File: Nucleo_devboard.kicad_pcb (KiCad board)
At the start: 4 copper layers, 70 x 82.5 mm, 62 parts, among them J2 Conn_ST_STDC14, J3 USB_5V, J4 E5V, J5 Curr_measure, J6 USB4105-GF-A, SW2 BOOT0 pull, U1 STM32G474RETx, U2 USBLC6-2SC6, U3 CP2102C-Axx-xQFN24, U4 NUCLEO-G474RE, U5 TLV75533PDBV, Y1 Crystal 24MHz, Y2 Crystal 32.768KHz

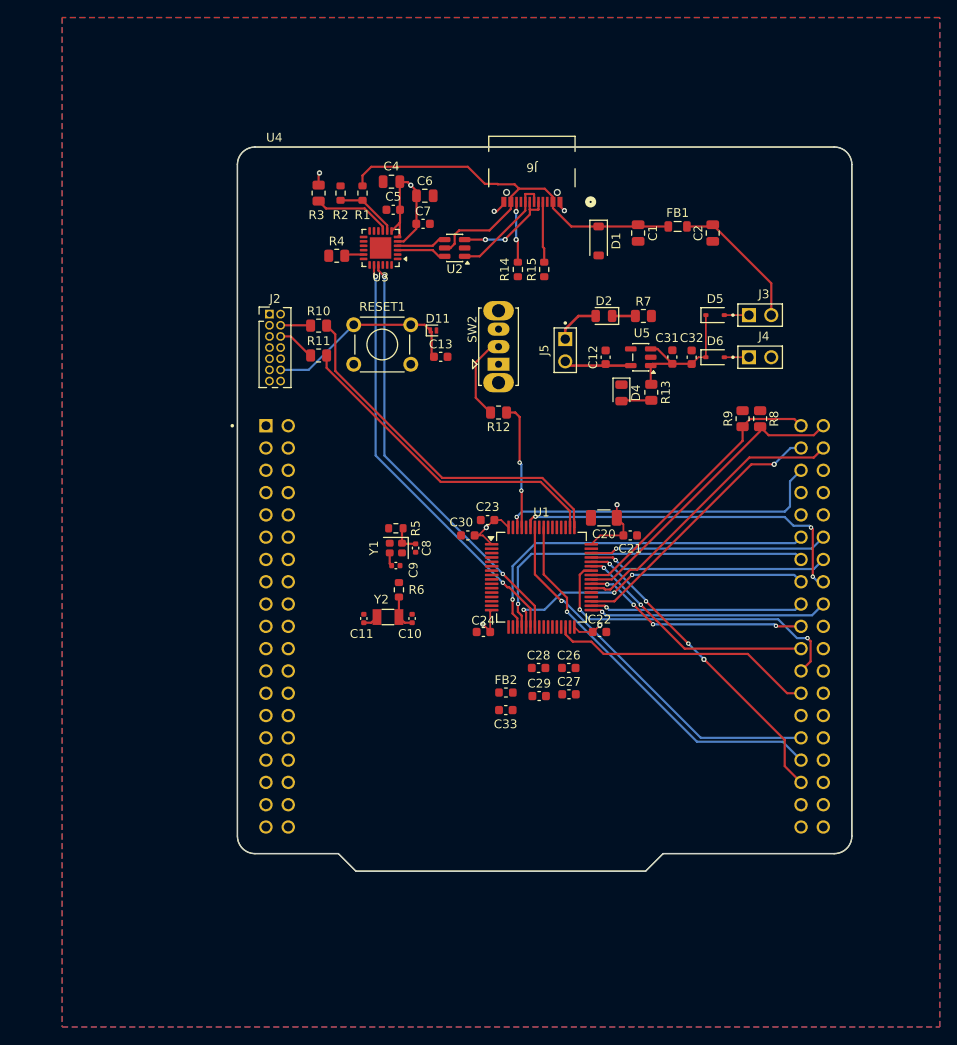
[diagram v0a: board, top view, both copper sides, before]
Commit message: Added Current reading for INA228 Started rev 02 on brake sense
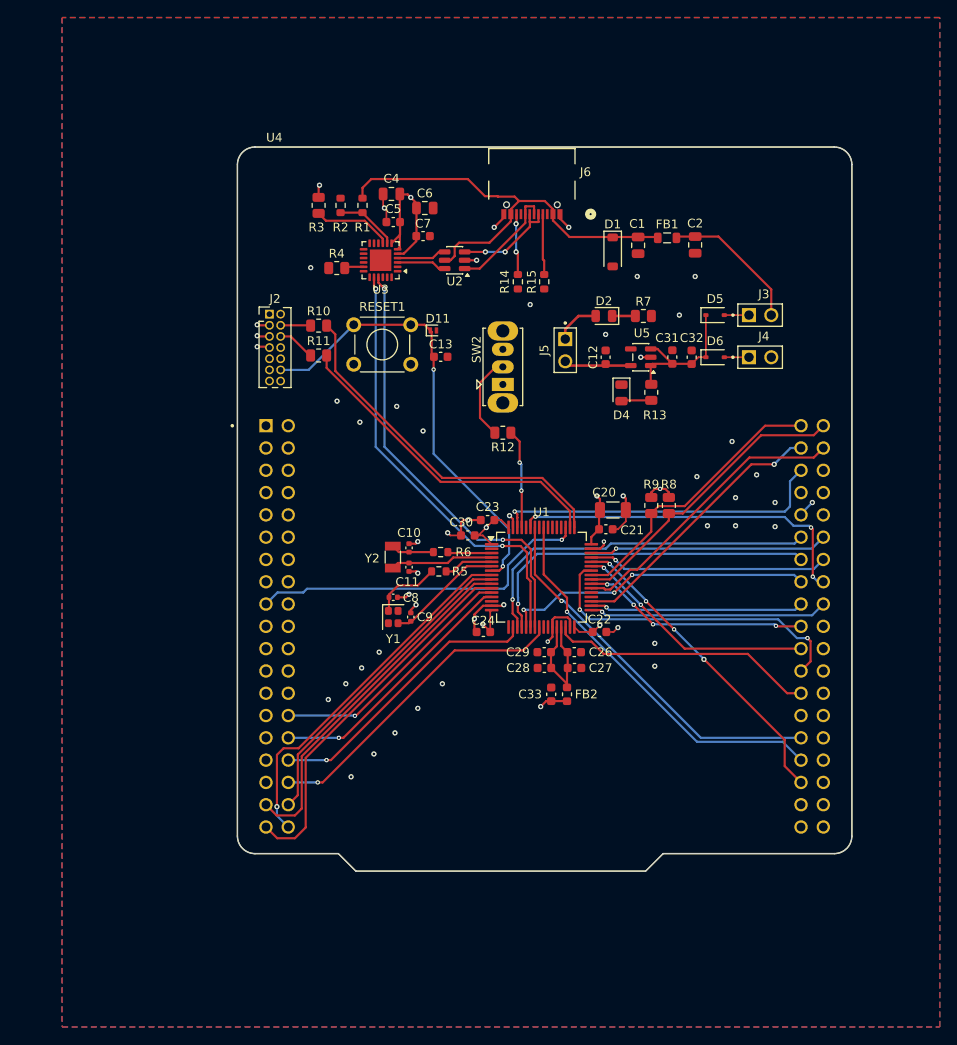
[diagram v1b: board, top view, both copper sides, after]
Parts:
- moved R8 14.4 mm to (155.4, 104.1)
- moved R9 14.4 mm to (153.4, 104.1)
- moved C10 8.05 mm to (125.8, 108.9)
- moved Y1 7.87 mm to (124.0, 116.8), turned to -90 degrees
- moved C11 7.79 mm to (125.8, 111.1), turned to 90 degrees
- moved FB2 6.97 mm to (143.8, 125.6), turned to 90 degrees
- moved R5 6.94 mm to (129.2, 111.6), turned to 0 degrees
- moved Y2 6.85 mm to (124.0, 110.0), turned to 90 degrees
- moved R6 6.40 mm to (129.4, 109.4), turned to 0 degrees
- moved C8 6.16 mm to (124.0, 114.5), turned to 180 degrees
- moved C9 6.10 mm to (126.0, 116.8), turned to -90 degrees
- moved C33 5.48 mm to (142.0, 125.6), turned to 90 degrees
- moved C29 5.03 mm to (141.2, 120.8), turned to 180 degrees
- moved C27 3.06 mm to (144.7, 122.6)
- moved C21 2.86 mm to (148.2, 106.8)
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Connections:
- R8 pad 2: GND -> +3V3
- R9 pad 2: GND -> +3V3
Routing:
- net GND: track 2.91 -> 46.7 mm, vias 2 -> 42
- net /MCU/SNS_ARMREST: track 0.00 -> 42.7 mm
- net /MCU/EN_ARMREST: track 0.00 -> 41.7 mm, vias 0 -> 1
- net /MCU/BTN_CDC: track 0.00 -> 40.6 mm
- net /MCU/FD_CAN3_TX: track 0.00 -> 39.6 mm, vias 0 -> 1
- net /MCU/EN_CDC: track 0.00 -> 36.5 mm
- net /MCU/ADC_LIFT_A: track 0.00 -> 36.4 mm, vias 0 -> 1
- net /MCU/ADC_TILT_A: track 0.00 -> 32.5 mm, vias 0 -> 1
- net /MCU/ADC_STEER_A: track 0.00 -> 29.8 mm, vias 0 -> 1
- net /MCU/NRST: track 22.6 -> 51.9 mm, vias 0 -> 2
- net /MCU/ADC_THROTTLE_A: track 0.00 -> 29.0 mm, vias 0 -> 1
- net VDDA: track 0.00 -> 15.1 mm
- net /MCU/HSE_OUT: track 1.54 -> 13.4 mm
- net /MCU/LSE_OUT: track 1.77 -> 11.8 mm
- net +3V3: track 46.2 -> 52.5 mm, vias 6 -> 17
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
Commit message: added rev04_mcu1/2.h revised brake sense board Added logic for 2 MCUs on nucleo board
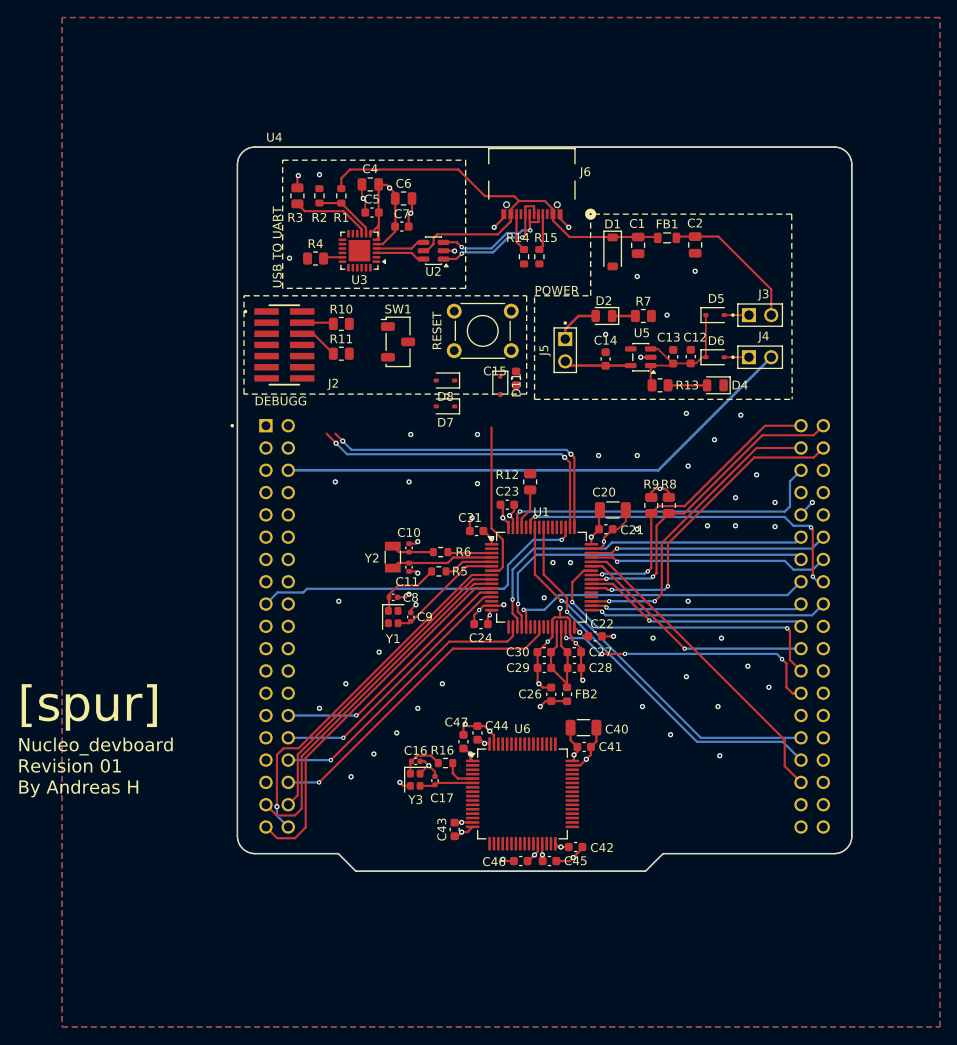
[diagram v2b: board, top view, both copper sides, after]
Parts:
- removed the C31 at (155.8, 87.2)
- removed C32: 1μF, Capacitor_SMD:C_0603_1608Metric
- removed SW2: BOOT0 pull, Button_Switch_THT:SW_Slide_SPDT_Straight_CK_OS102011MS2Q
- added C13: 100nF, Capacitor_SMD:C_0603_1608Metric, F.Cu at (155.9, 87.2)
- added C14: 1μF, Capacitor_SMD:C_0603_1608Metric, F.Cu at (148.2, 87.4)
- added C16: 6.8pF, Capacitor_SMD:C_0402_1005Metric, F.Cu at (126.6, 133.2)
- added C17: 6.8pF, Capacitor_SMD:C_0402_1005Metric, F.Cu at (128.8, 135.4)
- added C40: 10μF, Capacitor_SMD:C_1206_3216Metric, F.Cu at (145.7, 129.4)
- added C41: 100nF, Capacitor_SMD:C_0603_1608Metric, F.Cu at (145.8, 131.6)
- added C42: 100nF, Capacitor_SMD:C_0603_1608Metric, F.Cu at (144.8, 143.0)
- added C43: 100nF, Capacitor_SMD:C_0603_1608Metric, F.Cu at (131.0, 141.0)
- added C44: 100nF, Capacitor_SMD:C_0603_1608Metric, F.Cu at (133.6, 130.0)
- added C45: 100nF, Capacitor_SMD:C_0603_1608Metric, F.Cu at (141.8, 144.6)
- added C46: 100nF, Capacitor_SMD:C_0603_1608Metric, F.Cu at (138.5, 144.6)
- added C47: 100nF, Capacitor_SMD:C_0603_1608Metric, F.Cu at (132.0, 131.0)
- added D7: BAT60A, Diode_SMD:D_SOD-323, F.Cu at (129.9, 92.8)
- added D8: BAT60A, Diode_SMD:D_SOD-323, F.Cu at (129.9, 89.8)
- added R16: 0, Resistor_SMD:R_0603_1608Metric, F.Cu at (130.0, 133.4)
- added SW1: SW_Nidec_CAS-120A1, Button_Switch_SMD:Nidec_Copal_CAS-120A, F.Cu at (124.5, 85.5)
- added U6: STM32G474RETx, Package_QFP:LQFP-64_10x10mm_P0.5mm, F.Cu at (138.7, 136.9)
- added Y3: Crystal 24MHz, Crystal:Crystal_SMD_2016-4Pin_2.0x1.6mm, F.Cu at (126.5, 135.3)
- D11: value PESD3V3U1UL -> CDSOD323-T03; footprint Diode_SMD:D_SOD-882 -> Diode_SMD:D_SOD-323
- D5, D6: value SS34 -> BAT60A
- J2: value Conn_ST_STDC14 -> st_debug_SMD; footprint Connector_PinHeader_1.27mm:PinHeader_2x07_P1.27mm_Vertical -> tinynav:PinHeader_2x07_P1.27mm_Vertical_SMD
- moved RESET1 11.6 mm to (130.9, 82.0)
- moved D4 10.7 mm to (160.7, 90.4), turned to 180 degrees
- moved D11 9.86 mm to (136.2, 90.4), turned to -90 degrees
- moved C12 9.70 mm to (157.9, 87.1)
- moved C15 8.93 mm to (138.0, 89.6), turned to -90 degrees
- moved R12 6.41 mm to (139.6, 101.4), turned to 90 degrees
- moved J2 3.90 mm to (111.6, 85.8), turned to -90 degrees
- moved R14 2.93 mm to (138.9, 75.8)
- moved R15 2.90 mm to (140.7, 75.8)
- moved C23 2.85 mm to (137.0, 104.0), turned to 0 degrees
- moved C7 2.65 mm to (125.0, 72.3)
- moved C6 2.65 mm to (125.2, 69.1)
- moved R1 2.65 mm to (118.1, 68.8)
- moved R2 2.65 mm to (115.6, 68.8)
- moved R3 2.65 mm to (113.1, 68.8)
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- renumbered C13 to C15, C33 to C26, C26 to C27, C27 to C28, C28 to C29, C29 to C30, C30 to C31
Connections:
- net /MCU/E5V renamed /Morpho connector/E5V
- net /MCU/SWCLK renamed MCU2_SWDCLK
- net /MCU/USB/USB_5V renamed /Power/USB_5V
- net /MCU/USB/VBUS_DETECT renamed /USB/VBUS_DETECT
- C12 pad 1: /MCU/3.3V_OUT -> +5V
- J2 pad 11: unconnected-(J2-GNDDetect-Pad11) -> GND
- J5 pad 2: /MCU/3.3V_OUT -> /Power/3.3V_OUT
- R10 pad 2: /MCU/SWDIO -> Net-(SW1-B)
- R12 pad 2: Net-(SW2-B) -> GND
- RESET1 pad 1: /MCU/NRST -> Net-(D7-K)
- U1 pad 22: USART1_TX -> /MCU/USART_1TX
- U1 pad 23: USART1_RX -> /MCU/USART1_RX
- U1 pad 52: unconnected-(U1-PC10-Pad52) -> /MCU/USART3_TX
- U1 pad 53: unconnected-(U1-PC11-Pad53) -> /MCU/USART3_RX
- U3 pad 20: USART1_TX -> /MCU/USART3_RX
- U3 pad 21: USART1_RX -> /MCU/USART3_TX
- U5 pad 5: /MCU/3.3V_OUT -> /Power/3.3V_OUT
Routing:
- net USART1_TX: track 50.3 -> 0.00 mm, vias 2 -> 0
- net USART1_RX: track 50.2 -> 0.00 mm, vias 2 -> 0
- net GND: track 46.7 -> 82.7 mm, vias 42 -> 76
- net /MCU/NRST: track 51.9 -> 17.9 mm, vias 2 -> 0
- net Net-(SW2-B): track 9.74 -> 0.00 mm
- net +3V3: track 52.5 -> 60.3 mm, vias 17 -> 16
- net /Power/3.3V_OUT: track 0.00 -> 7.66 mm
- net /MCU/3.3V_OUT: track 7.66 -> 0.00 mm
- net /MCU/BOOT: track 11.3 -> 4.67 mm, vias 2 -> 0
- net /MCU 2/HSE_OUT: track 0.00 -> 6.13 mm
- net Net-(C16-Pad2): track 0.00 -> 5.12 mm
- net /MCU/SWDIO: track 41.4 -> 36.3 mm, vias 0 -> 2
- net VBUS: track 51.4 -> 56.1 mm
- net /MCU 2/HSE_IN: track 0.00 -> 3.68 mm
- net /MCU/EN_PARK_N: track 31.1 -> 34.6 mm, vias 1 -> 2
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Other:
- board text added: "DEBUGG"
- board text added: "Nucleo_devboard Revision 01 By Andreas H"
- board text added: "POWER"
- board text added: "RESET"
- board text added: "USB TO UART"
- board text added: "[spur]"

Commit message: Generated scaffold for mcu2 finished brake sense rev2 finished adding second chip to nucleo devboard
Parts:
- removed SW1: SW_Nidec_CAS-120A1, Button_Switch_SMD:Nidec_Copal_CAS-120A
- added C18: 100nF, Capacitor_SMD:C_0603_1608Metric, F.Cu at (133.0, 129.8)
- added C50: 100nF, Capacitor_SMD:C_0603_1608Metric, F.Cu at (152.0, 139.4)
- added C51: 100nF, Capacitor_SMD:C_0603_1608Metric, F.Cu at (155.4, 139.4)
- added D12: CDSOD323-T03, Diode_SMD:D_SOD-323, F.Cu at (127.8, 89.4)
- added J1: st_debug_SMD, tinynav:PinHeader_2x07_P1.27mm_Vertical_SMD, F.Cu at (111.2, 74.8)
- added J7: Conn_01x03_Socket, tinynav:DF3-3P-2DSA, F.Cu at (162.9, 136.5)
- added J8: CAN, tinynav:HARWIN_M20-9990246, F.Cu at (159.2, 135.2)
- added R17: 47, Resistor_SMD:R_0805_2012Metric, F.Cu at (118.1, 87.1)
- added R18: 47, Resistor_SMD:R_0805_2012Metric, F.Cu at (118.1, 89.4)
- added R29: 120, Resistor_SMD:R_0805_2012Metric, F.Cu at (159.2, 139.2)
- added U7: MCP2562-E-SN, Package_SO:SOIC-8_3.9x4.9mm_P1.27mm, F.Cu at (153.6, 135.8)
- RESET1: value SW_SPST -> RST_button
- moved C15 15.0 mm to (133.7, 104.0), turned to 180 degrees
- moved D11 11.6 mm to (127.8, 82.4), turned to 0 degrees
- moved D7 8.30 mm to (127.8, 84.8)
- moved R3 6.22 mm to (119.3, 68.6)
- moved C6 5.90 mm to (131.1, 69.0)
- moved C4 5.90 mm to (127.3, 67.4)
- moved C5 5.90 mm to (127.5, 70.6)
- moved C7 5.90 mm to (130.9, 72.2)
- moved R1 5.90 mm to (124.0, 68.7)
- moved R2 5.90 mm to (121.5, 68.7)
- moved R4 5.90 mm to (121.0, 75.9)
- moved U3 5.90 mm to (126.0, 75.0)
- moved FB1 4.84 mm to (154.2, 78.3), turned to -90 degrees
- moved C2 4.39 mm to (156.6, 78.4), turned to 90 degrees
- moved C1 3.91 mm to (151.6, 78.3)
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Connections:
- net /MCU/ADC_BRAKE renamed /MCU 1/ADC_BRAKE
- net /MCU/ADC_LIFT_A renamed /MCU 1/ADC_LIFT_A
- net /MCU/ADC_STEER_A renamed /MCU 1/ADC_STEER_A
- net /MCU/ADC_THROTTLE_A renamed /MCU 1/ADC_THROTTLE_A
- net /MCU/ADC_TILT_A renamed /MCU 1/ADC_TILT_A
- net /MCU/BTN_CDC renamed /MCU 1/BTN_CDC
- net /MCU/BTN_FNR_F renamed /MCU 1/BTN_FNR_F
- net /MCU/BTN_FNR_R renamed /MCU 1/BTN_FNR_R
- net /MCU/BTN_KICK renamed /MCU 1/BTN_KICK
- net /MCU/EN_ARMREST renamed /MCU 1/EN_ARMREST
- net /MCU/EN_CDC renamed /MCU 1/EN_CDC
- net /MCU/EN_FNR_F renamed /MCU 1/EN_FNR_F
- net /MCU/EN_FNR_R renamed /MCU 1/EN_FNR_R
- net /MCU/EN_KICK renamed /MCU 1/EN_KICK
- net /MCU/FDCAN2_TX renamed /MCU 1/FDCAN2_TX
- net /MCU/FD_CAN1_RX renamed /MCU 1/FD_CAN1_RX
- net /MCU/FD_CAN1_TX renamed /MCU 1/FD_CAN1_TX
- net /MCU/FD_CAN2_RX renamed /MCU 1/FD_CAN2_RX
- net /MCU/FD_CAN3_RX renamed /MCU 1/FD_CAN3_RX
- net /MCU/FD_CAN3_TX renamed /MCU 1/FD_CAN3_TX
- net /MCU/HSE_IN renamed /MCU 1/HSE_IN
- net /MCU/HSE_OUT renamed /MCU 1/HSE_OUT
- net /MCU/I2C_SCL renamed /MCU 1/I2C_SCL
- net /MCU/I2C_SDA renamed /MCU 1/I2C_SDA
- net /MCU/LDAC_LIFT_TILT renamed /MCU 1/LDAC_LIFT_TILT
- net /MCU/LDAC_STEER renamed /MCU 1/LDAC_STEER
- net /MCU/LDAC_THROTTLE renamed /MCU 1/LDAC_THROTTLE
- net /MCU/LSE_IN renamed /MCU 1/LSE_IN
- net /MCU/LSE_OUT renamed /MCU 1/LSE_OUT
- net /MCU/PWM_BRAKE renamed /MCU 1/PWM_BRAKE
- net /MCU/SEL_INJECT renamed /MCU 1/SEL_INJECT
- net /MCU/SNS_ARMREST renamed /MCU 1/SNS_ARMREST
- net /MCU/USART3_RX renamed /MCU 1/USART3_RX
- net /MCU/USART3_TX renamed /MCU 1/USART3_TX
- net MCU2_SWDCLK renamed /MCU 1/SWCLK1
- C15 pad 1: /MCU/NRST -> /MCU 1/NRST
- D11 pad 1: /MCU/NRST -> /MCU 1/NRST
- D7 pad 2: /MCU/NRST -> /MCU 1/NRST
- D8 pad 2: MCU2_rst -> /MCU 2/NRST
- J2 pad 12: /MCU/NRST -> /MCU 2/NRST
- R10 pad 1: Net-(J2-JTMS/SWDIO) -> Net-(J1-JTMS/SWDIO)
- R10 pad 2: Net-(SW1-B) -> /MCU 1/SWDIO1
- R11 pad 1: Net-(J2-JCLK/SWCLK) -> Net-(J1-JCLK/SWCLK)
- R12 pad 1: /MCU/BOOT -> /MCU 1/BOOT
- U1 pad 22: /MCU/USART_1TX -> /MCU 1/USART_1TX
- U1 pad 23: /MCU/USART1_RX -> /MCU 1/USART1_RX
- U1 pad 35: /MCU/EN_PARK_N -> unconnected-(U1-PB13-Pad35)
- U1 pad 49: /MCU/SWDIO -> /MCU 1/SWDIO1
- U1 pad 61: /MCU/BOOT -> /MCU 1/BOOT
- U1 pad 7: /MCU/NRST -> /MCU 1/NRST
- U4 pad CN10_3: /MCU/EN_PARK_N -> /MCU 1/BOOT
- U4 pad CN7_16: +3.3V -> +3V3
- U6 pad 45: unconnected-(U6-PA11-Pad45) -> /MCU 2/FC_CAN1_RX
- U6 pad 46: unconnected-(U6-PA12-Pad46) -> /MCU 2/FC_CAN1_TX
- U6 pad 49: unconnected-(U6-PA13-Pad49) -> /MCU 2/SWDIO2
- U6 pad 50: unconnected-(U6-PA14-Pad50) -> /MCU 2/SWCLK2
- U6 pad 52: unconnected-(U6-PC10-Pad52) -> /MCU 1/USART1_RX
- U6 pad 53: unconnected-(U6-PC11-Pad53) -> /MCU 1/USART_1TX
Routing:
- net +5V: track 16.8 -> 107.5 mm, vias 0 -> 2
- net /MCU 2/NRST: track 0.00 -> 74.1 mm, vias 0 -> 5
- net /MCU 2/SWDIO2: track 0.00 -> 65.3 mm, vias 0 -> 2
- net /MCU 2/SWCLK2: track 0.00 -> 62.4 mm, vias 0 -> 2
- net /MCU 1/NRST: track 0.00 -> 57.9 mm, vias 0 -> 4
- net /MCU 1/SWDIO1: track 0.00 -> 48.2 mm, vias 0 -> 2
- net /MCU 1/USART3_TX: track 0.00 -> 45.3 mm, vias 0 -> 2
- net /MCU 1/USART3_RX: track 0.00 -> 45.2 mm, vias 0 -> 2
- net GND: track 82.7 -> 122.1 mm, vias 76 -> 102
- net /MCU 1/BOOT: track 0.00 -> 37.5 mm, vias 0 -> 1
- net /MCU/SWDIO: track 36.3 -> 0.00 mm, vias 2 -> 0
- net /MCU/EN_PARK_N: track 34.6 -> 0.00 mm, vias 2 -> 0
- net /MCU/NRST: track 17.9 -> 0.00 mm
- net /MCU 1/USART_1TX: track 0.00 -> 15.4 mm, vias 0 -> 2
- net /MCU 1/USART1_RX: track 0.00 -> 15.0 mm, vias 0 -> 2
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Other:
- board text added: "3V3"
- board text added: "5V"
- board text added: "DEBUG"
- board text added: "E5V"
- board text added: "GND|L|H"
- board text added: "MCU1"
- board text added: "MCU2"
- board text added: "MCU2 CAN"
- board text added: "USB_5V"
- board text removed: "DEBUGG"

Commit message: Finished last thouches on brake sense and nucleo pcb (Ordered pcbs)
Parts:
- added D8: APT2012CGCK, LED_SMD:LED_0805_2012Metric, F.Cu at (159.3, 115.1)
- added G***: LOGO, LOGO, B.Cu at (134.0, 133.2)
- added R19: 560, Resistor_SMD:R_0805_2012Metric, F.Cu at (163.3, 115.1)
- D11, D12: value CDSOD323-T03 -> STS321033B401
- R10, R11, R17, R18: footprint Resistor_SMD:R_0805_2012Metric -> Resistor_SMD:R_0603_1608Metric
- moved D11 2.40 mm to (127.7, 84.8)
- moved D6 2.30 mm to (127.7, 82.5)
- renumbered D5 to D2, D6 to D3, D2 to D5, D7 to D6, D8 to D7
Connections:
- U1 pad 35: unconnected-(U1-PB13-Pad35) -> Net-(D8-A)
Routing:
- net Net-(D8-A): track 0.00 -> 11.9 mm, vias 0 -> 2
- net GND: track 122.1 -> 127.9 mm, vias 102 -> 104
- net Net-(D6-K): track 12.6 -> 15.0 mm
- net /MCU 1/NRST: track 57.9 -> 55.6 mm
- net Net-(D8-K): track 0.00 -> 2.15 mm
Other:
- board text added: "LED test"

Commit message: volvo_h2 revision Revised switch regulator layout/components Changed brake circuit to use current sense amplifier Defined nets and nettclass constraints. Revises trace layout to fit new constraints.
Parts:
- J3, J4, J5, J8: footprint tinynav:HARWIN_M20-9990246 -> tinynav:jumper_header
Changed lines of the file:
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@@
 		)
 	)
-	(footprint "tinynav:HARWIN_M20-9990246"
+	(footprint "tinynav:jumper_header"
 		(layer "F.Cu")
 		(at 165.8 82.4)
@@
 		)
 		(embedded_fonts no)
-		(model "../../libs/3dmodels/M20-9990246.step"
+		(model "../../libs/3dmodels/jumper_header.step"
 			(offset
 				(xyz 0 0 0)
@@
 		)
 	)
-	(footprint "tinynav:HARWIN_M20-9990246"
+	(footprint "tinynav:jumper_header"
 		(layer "F.Cu")
 		(at 159.150001 135.235 -90)
@@
 		)
 		(embedded_fonts no)
-		(model "../../libs/3dmodels/M20-9990246.step"
+		(model "../../libs/3dmodels/jumper_header.step"
 			(offset
 				(xyz 0 0 0)
@@
 		)
 	)
-	(footprint "tinynav:HARWIN_M20-9990246"
+	(footprint "tinynav:jumper_header"
 		(layer "F.Cu")
 		(at 143.6 86.4 -90)
@@
 		)
 		(embedded_fonts no)
-		(model "../../libs/3dmodels/M20-9990246.step"
+		(model "../../libs/3dmodels/jumper_header.step"
 			(offset
 				(xyz 0 0 0)
@@
 		)
 	)
-	(footprint "tinynav:HARWIN_M20-9990246"
+	(footprint "tinynav:jumper_header"
 		(layer "F.Cu")
 		(at 165.8 87.2)
@@
 		)
 		(embedded_fonts no)
-		(model "../../libs/3dmodels/M20-9990246.step"
+		(model "../../libs/3dmodels/jumper_header.step"
 			(offset
 				(xyz 0 0 0)
